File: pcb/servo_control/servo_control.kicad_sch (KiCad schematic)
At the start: 11 parts, among them J1 USB_B_Micro, J2 Conn_01x03, J3 Conn_01x03, J4 Conn_01x03, J5 Conn_01x03, J6 Conn_01x03, J7 Conn_01x03, J8 Conn_01x03, J9 Conn_01x03, U1 ATmega2560-16A

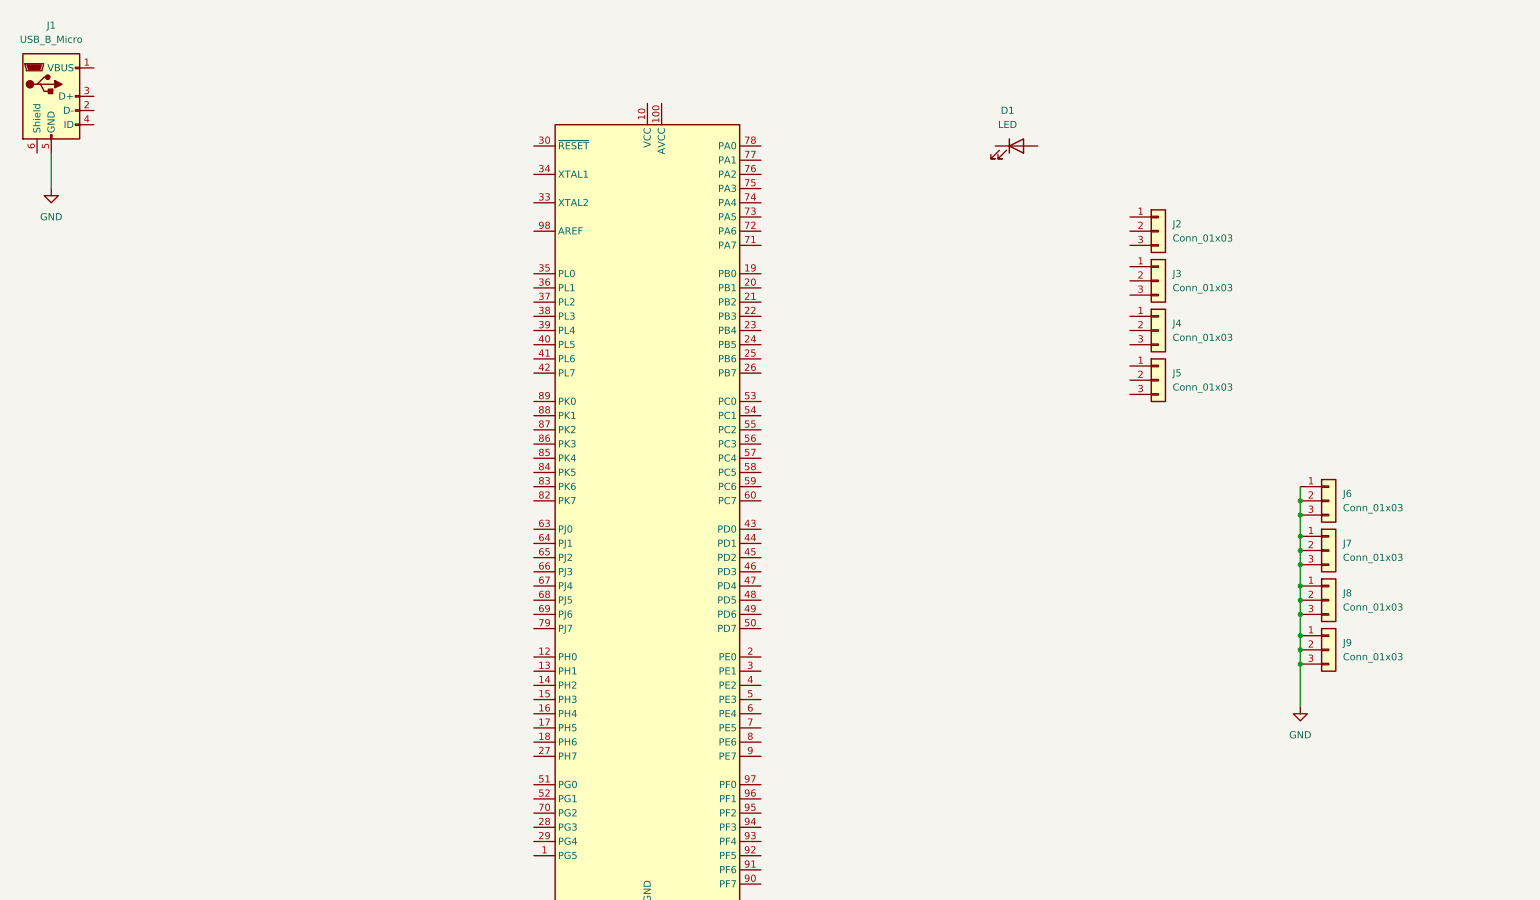
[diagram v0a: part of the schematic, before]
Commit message: add legs connector
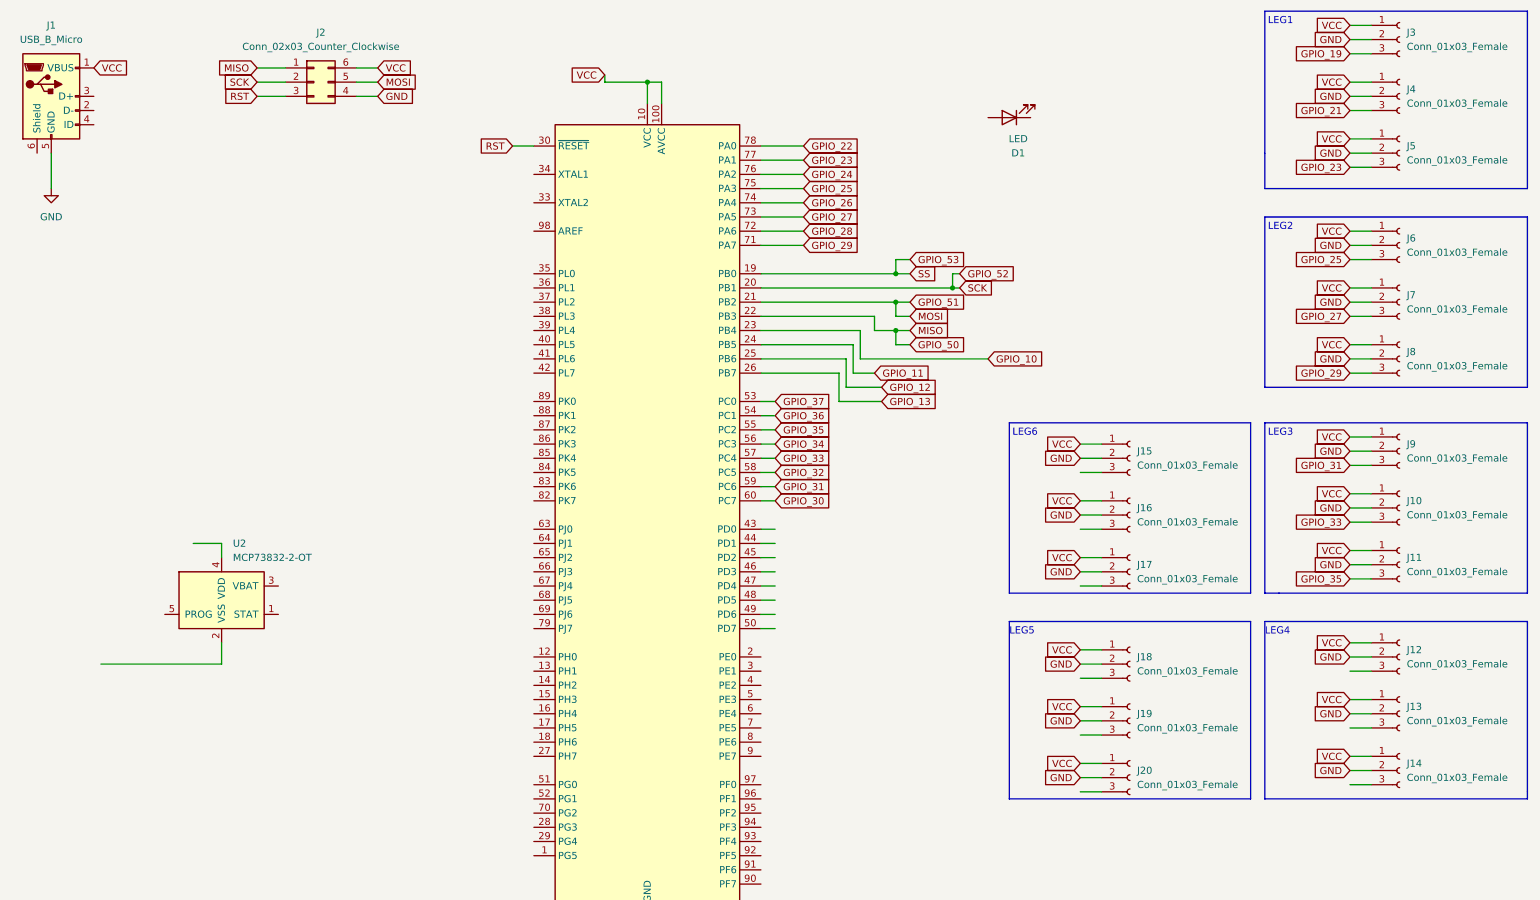
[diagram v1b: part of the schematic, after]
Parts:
- removed J2, J3, J4, J5, J6, J7, J8, J9: Conn_01x03, Connector:FanPinHeader_1x03_P2.54mm_Vertical, symbol Connector_Generic:Conn_01x03
- added J10, J11, J12, J13, J14, J15, J16, J17, J18, J19, J20, J3, J4, J5, J6, J7, J8, J9: Conn_01x03_Female, Connector_PinHeader_2.54mm:PinHeader_1x03_P2.54mm_Vertical, symbol Connector:Conn_01x03_Female
- added J2: Conn_02x03_Counter_Clockwise, Connector_PinHeader_2.54mm:PinHeader_2x03_P2.54mm_Vertical, symbol Connector_Generic:Conn_02x03_Counter_Clockwise
- added U2: MCP73832-2-OT, Package_TO_SOT_SMD:SOT-23-5, symbol Battery_Management:MCP73832-2-OT
- J1: footprint Connector_USB:USB3_A_Molex_48393-001 -> Connector_USB:USB_Micro-B_Molex-105017-0001
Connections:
- net GND: now also J10.2 (Pin_2), J11.2 (Pin_2), J12.2 (Pin_2), J13.2 (Pin_2), J14.2 (Pin_2), J15.2 (Pin_2), J16.2 (Pin_2), J17.2 (Pin_2), J18.2 (Pin_2), J19.2 (Pin_2), J2.4 (Pin_4), J20.2 (Pin_2), J3.2 (Pin_2), J4.2 (Pin_2), J5.2 (Pin_2), J6.2 (Pin_2), J7.2 (Pin_2), J8.2 (Pin_2), J9.2 (Pin_2)
- net VCC: now reaches U1.10 (VCC), U1.31 (VCC), U1.61 (VCC), U1.80 (VCC)
- net VCC: now also J1.1 (VBUS), U1.100 (AVCC), J10.1 (Pin_1), J11.1 (Pin_1), J12.1 (Pin_1), J13.1 (Pin_1), J14.1 (Pin_1), J15.1 (Pin_1), J16.1 (Pin_1), J17.1 (Pin_1), J18.1 (Pin_1), J19.1 (Pin_1), J2.6 (Pin_6), J20.1 (Pin_1), J3.1 (Pin_1), J4.1 (Pin_1), J5.1 (Pin_1), J6.1 (Pin_1), J7.1 (Pin_1), J8.1 (Pin_1), J9.1 (Pin_1)
- net GPIO_53: now reaches U1.19 (PB0)
- net GPIO_52: now reaches U1.20 (PB1)
- net GPIO_52: now also J2.2 (Pin_2)
- net GPIO_51: now reaches U1.21 (PB2)
- net GPIO_51: now also J2.5 (Pin_5)
- net GPIO_50: now reaches U1.22 (PB3)
- net GPIO_50: now also J2.1 (Pin_1)
- net GPIO_10: now reaches U1.23 (PB4)
- net GPIO_11: now reaches U1.24 (PB5)
- net GPIO_12: now reaches U1.25 (PB6)
- net GPIO_13: now reaches U1.26 (PB7)
- net RST: now reaches U1.30 (~{RESET})
- net RST: now also J2.3 (Pin_3)
- net GPIO_37: now reaches U1.53 (PC0)
- net GPIO_36: now reaches U1.54 (PC1)
- net GPIO_35: now reaches U1.55 (PC2)
- net GPIO_35: now also J11.3 (Pin_3)
- net GPIO_34: now reaches U1.56 (PC3)
- net GPIO_33: now reaches U1.57 (PC4)
- net GPIO_33: now also J10.3 (Pin_3)
- net GPIO_32: now reaches U1.58 (PC5)
- net GPIO_31: now reaches U1.59 (PC6)
- net GPIO_31: now also J9.3 (Pin_3)
- net GPIO_30: now reaches U1.60 (PC7)
- net GPIO_29: now reaches U1.71 (PA7)
- net GPIO_29: now also J8.3 (Pin_3)
- net GPIO_28: now reaches U1.72 (PA6)
- net GPIO_27: now reaches U1.73 (PA5)
- net GPIO_27: now also J7.3 (Pin_3)
- net GPIO_26: now reaches U1.74 (PA4)
- net GPIO_25: now reaches U1.75 (PA3)
- net GPIO_25: now also J6.3 (Pin_3)
- net GPIO_24: now reaches U1.76 (PA2)
- net GPIO_23: now reaches U1.77 (PA1)
- net GPIO_23: now also J5.3 (Pin_3)
- net GPIO_22: now reaches U1.78 (PA0)
- new net GPIO_19: J3.3 (Pin_3)
- new net GPIO_21: J4.3 (Pin_3)
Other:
- note added: "LEG1"
- note added: "LEG2"
- note added: "LEG3"
- note added: "LEG4"
- note added: "LEG5"
- note added: "LEG6"
- moved on the sheet: D1

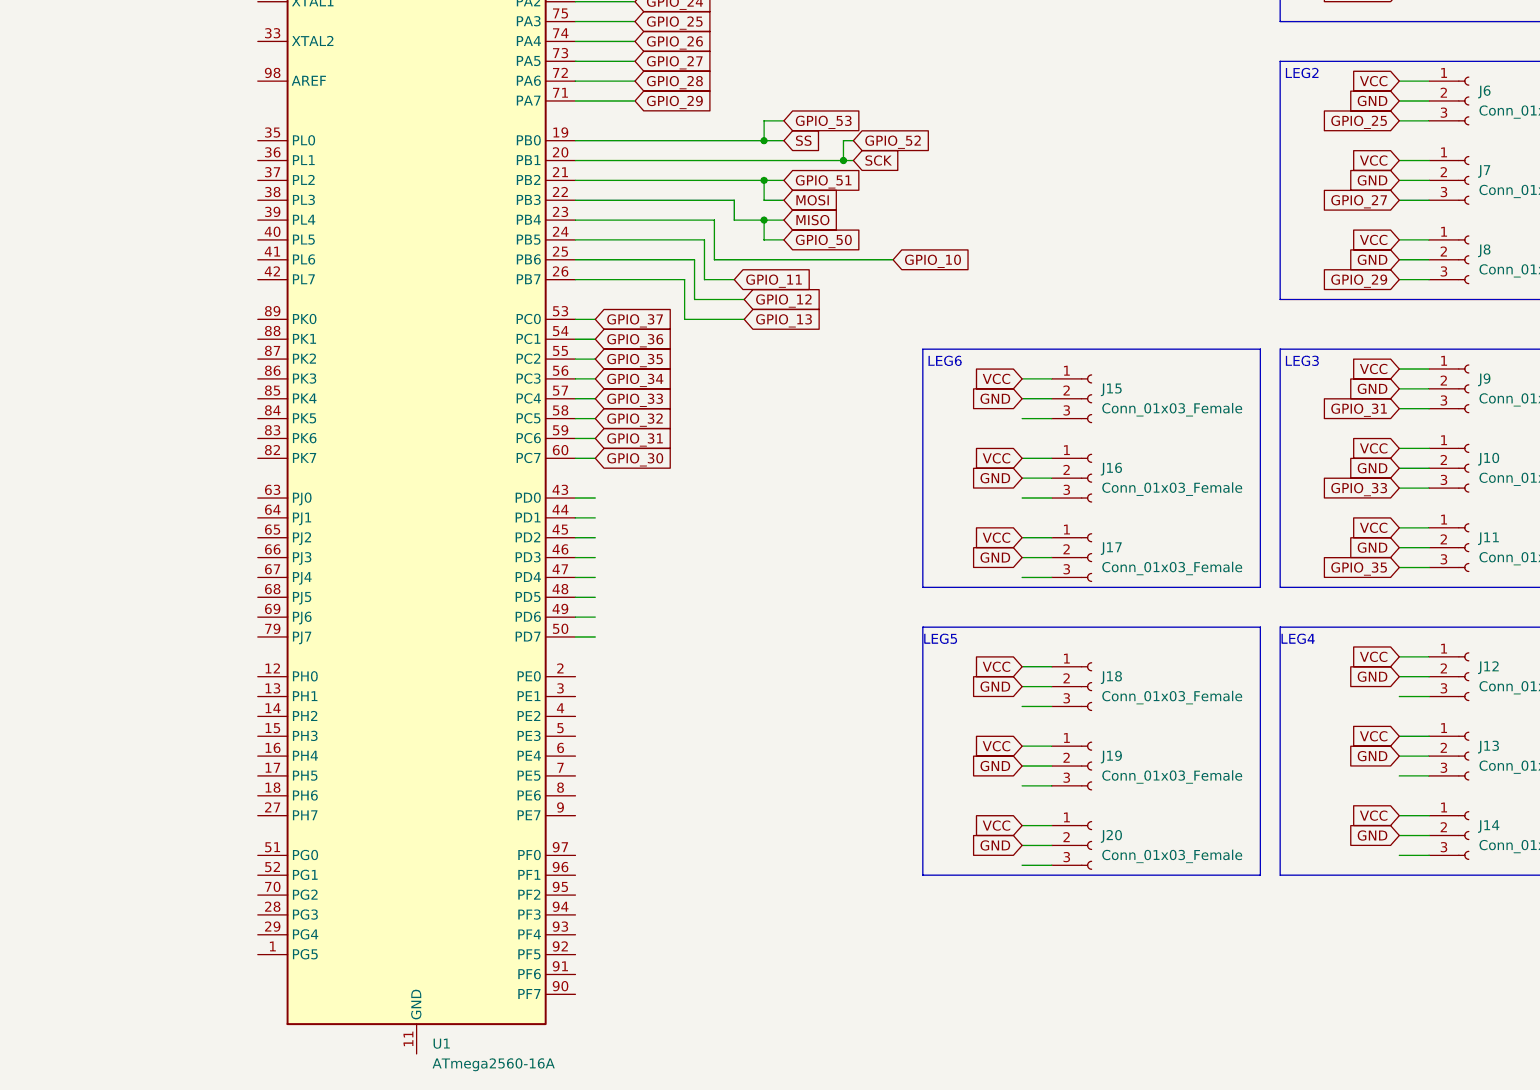
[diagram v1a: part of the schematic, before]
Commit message: all legs + add esp32 wroom on pcb
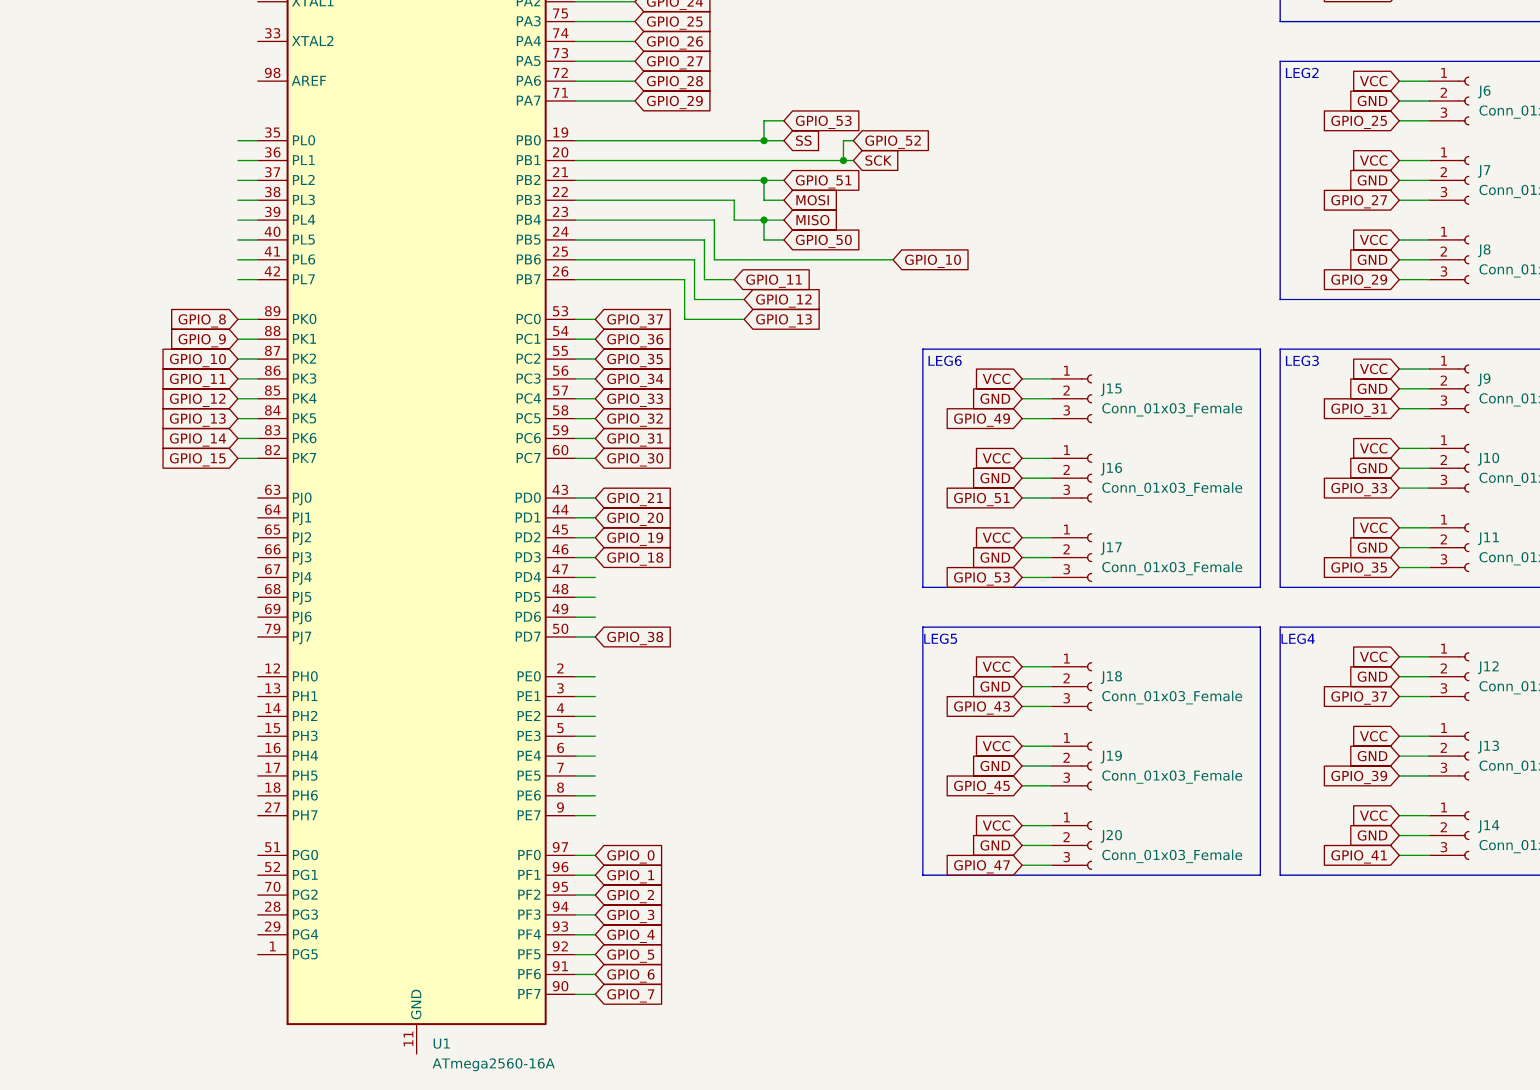
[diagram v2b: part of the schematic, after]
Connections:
- net GPIO_10: now also U1.87 (PK2)
- net GPIO_11: now also U1.86 (PK3)
- net GPIO_12: now also U1.85 (PK4)
- net GPIO_13: now also U1.84 (PK5)
- net GPIO_19: now also U1.45 (PD2)
- net GPIO_21: now also U1.43 (PD0)
- net GPIO_37: now also J12.3 (Pin_3)
- net GPIO_51: now also J16.3 (Pin_3)
- net GPIO_53: now also J17.3 (Pin_3)
- net GPIO_43: now reaches J18.3 (Pin_3)
- net GPIO_47: now reaches J20.3 (Pin_3)
- net GPIO_45: now reaches J19.3 (Pin_3)
- net GPIO_39: now reaches J13.3 (Pin_3)
- net GPIO_20: now reaches U1.44 (PD1)
- net GPIO_18: now reaches U1.46 (PD3)
- net GPIO_38: now reaches U1.50 (PD7)
- net GPIO_15: now reaches U1.82 (PK7)
- net GPIO_14: now reaches U1.83 (PK6)
- net GPIO_9: now reaches U1.88 (PK1)
- net GPIO_8: now reaches U1.89 (PK0)
- net GPIO_7: now reaches U1.90 (PF7)
- net GPIO_6: now reaches U1.91 (PF6)
- net GPIO_5: now reaches U1.92 (PF5)
- net GPIO_4: now reaches U1.93 (PF4)
- net GPIO_3: now reaches U1.94 (PF3)
- net GPIO_2: now reaches U1.95 (PF2)
- net GPIO_1: now reaches U1.96 (PF1)
- net GPIO_0: now reaches U1.97 (PF0)
- net GPIO_49: now reaches J15.3 (Pin_3)
- net GPIO_41: now reaches J14.3 (Pin_3)

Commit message: add ftdi
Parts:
- removed U2: MCP73832-2-OT, Package_TO_SOT_SMD:SOT-23-5, symbol Battery_Management:MCP73832-2-OT
- added C1: 1 uf, Capacitor_SMD:C_0603_1608Metric, symbol Device:C
- added C2: 1uf, Capacitor_SMD:C_0603_1608Metric, symbol Device:C
- added C3: 10 uf, Capacitor_SMD:C_0603_1608Metric, symbol Device:C
- added C? (x2): 0.1 uf, symbol Device:C
- added C?: 10 nf, symbol Device:C
- added D? (x2): LED, LED_SMD:LED_0603_1608Metric, symbol Device:LED
- added J?: Conn_01x06_Male, symbol Connector:Conn_01x06_Male
- added R? (x3): R, symbol Device:R
- added R? (x2): 4.7K, symbol Device:R
- added U2: LM317_SOT-223, Package_TO_SOT_SMD:SOT-223-3_TabPin2, symbol Regulator_Linear:LM317_SOT-223
- added U3: ESP32-WROOM-32, ESP32:MODULE_ESP32-WROOM-32, symbol ESP32-WROOM-32:ESP32-WROOM-32
- added U?: MPU-9250, Sensor_Motion:InvenSense_QFN-24_3x3mm_P0.4mm, symbol Sensor_Motion:MPU-9250
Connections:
- net GND: now also D1.1 (K), U1.11 (GND), U1.32 (GND), U1.62 (GND), U1.81 (GND), U1.99 (GND), C1.2, C2.2, C3.2, C?.2, C?.2, C?.2, D?.1 (K), D?.1 (K), J?.1 (Pin_1), U2.1 (ADJ), U3.1 (GND), U3.15 (GND), U3.38 (GND), U3.39_1 (GND), U3.39_10 (GND), U3.39_11 (GND), U3.39_12 (GND), U3.39_13 (GND), U3.39_14 (GND), U3.39_15 (GND), U3.39_16 (GND), U3.39_17 (GND), U3.39_18 (GND), U3.39_19 (GND), U3.39_2 (GND), U3.39_20 (GND), U3.39_21 (GND), U3.39_3 (GND), U3.39_4 (GND), U3.39_5 (GND), U3.39_6 (GND), U3.39_7 (GND), U3.39_8 (GND), U3.39_9 (GND), U?.18 (GND)
- net GPIO_39: now also U1.70 (PG2)
- net GPIO_41: now also U1.51 (PG0)
- net GPIO_43: now also U1.41 (PL6)
- net GPIO_45: now also U1.39 (PL4)
- net GPIO_47: now also U1.37 (PL2)
- net GPIO_49: now also U1.35 (PL0)
- net VCC: now also C1.1, U2.3 (VI)
- net GPIO_48: now reaches U1.36 (PL1)
- net GPIO_46: now reaches U1.38 (PL3)
- net GPIO_44: now reaches U1.40 (PL5)
- net GPIO_42: now reaches U1.42 (PL7)
- net GPIO_40: now reaches U1.52 (PG1)
- net at D1.2 (A): now also R?.2
- new net: D?.2 (A), R?.2 (x2)
- new net: C?.1, U?.10 (REGOUT)
- new net 3.3V: C2.1, C3.1, C?.1, C?.1, R?.2, R?.2, U2.2 (VO), U3.2 (3V3), U?.13 (VDD), U?.8 (VDDIO)
- new net FTDI_CTS: J?.2 (Pin_2)
- new net FTDI_RST: J?.6 (Pin_6)
- new net FTDI_RX: J?.5 (Pin_5), U3.35 (TXD0)
- new net FTDI_TX: J?.4 (Pin_4), U3.34 (RXD0)
- new net FTDI_VCC: J?.3 (Pin_3)
- new net I2C_SCL: R?.1, U3.36 (IO22), U?.23 (SCL/SCLK)
- new net I2C_SDA: R?.1, U3.33 (IO21), U?.24 (SDA/MOSI)
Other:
- note added: "3.3 regulator"
- note added: "ESP32-wroom"
- note added: "FTDI"
- note added: "ICSP PROGRAM"
- note added: "LED INDICATOR"
- moved on the sheet: D1, J1, J10, J11, J12, J13, J14, J15, J16, J17, J18, J19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
